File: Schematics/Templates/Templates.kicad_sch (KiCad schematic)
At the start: 2 parts, among them J1 Stack Male Edge Connector, U1 SAM-M8Q

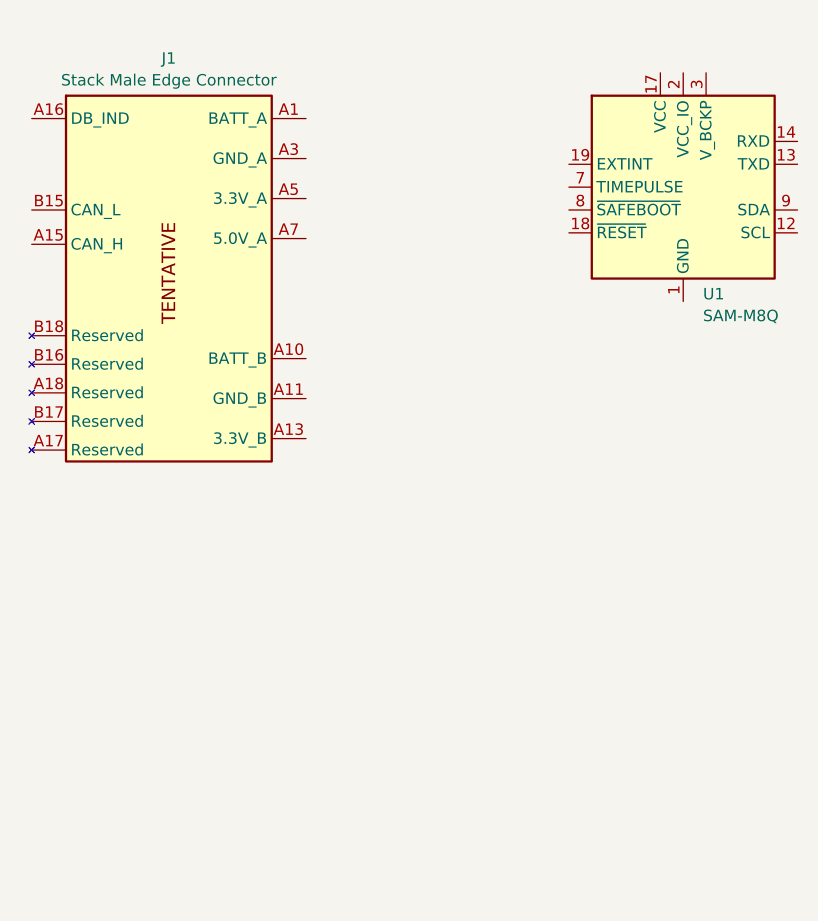
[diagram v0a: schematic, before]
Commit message: Added SWD programming header
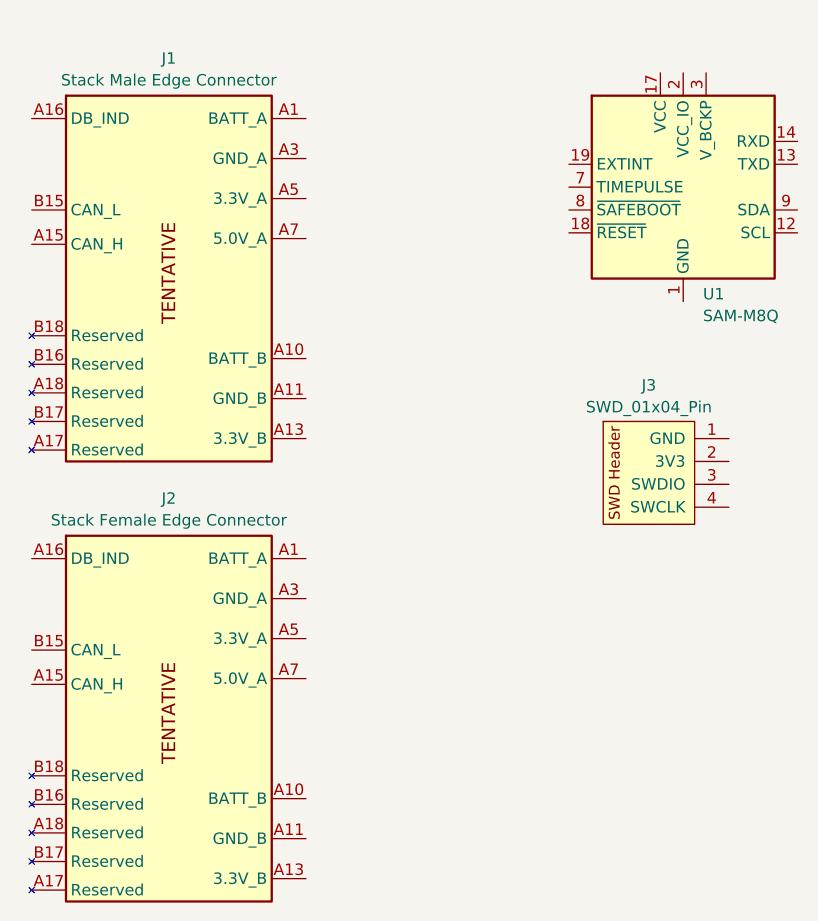
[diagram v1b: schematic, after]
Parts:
- added J2: Stack Female Edge Connector, footprints:CONN_10018784_AMP, symbol EdgeConnector:Stack Female Edge Connector
- added J3: SWD_01x04_Pin, SWD_Header:SWD_PinHeader_1x04_P2.54mm_Horizontal, symbol EdgeConnector:SWD_01x04_Pin
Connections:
- new net: J2.A1 (BATT_A), J2.A2 (BATT_A), J2.B1 (BATT_A), J2.B2 (BATT_A)
- new net: J2.A10 (BATT_B), J2.A9 (BATT_B), J2.B10 (BATT_B), J2.B9 (BATT_B)
- new net: J2.A11 (GND_B), J2.A12 (GND_B), J2.A14 (GND_B), J2.B11 (GND_B), J2.B12 (GND_B), J2.B14 (GND_B)
- new net: J2.A13 (3.3V_B), J2.B13 (3.3V_B)
- new net: J2.A3 (GND_A), J2.A4 (GND_A), J2.A6 (GND_A), J2.A8 (GND_A), J2.B3 (GND_A), J2.B4 (GND_A), J2.B6 (GND_A), J2.B8 (GND_A)
- new net: J2.A5 (3.3V_A), J2.B5 (3.3V_A)
- new net: J2.A7 (5.0V_A), J2.B7 (5.0V_A)
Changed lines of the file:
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@@
+    )
+  )
+  (symbol (lib_id "EdgeConnector:SWD_01x04_Pin") (at 107.95 67.31 0) (unit 1)
+    (in_bom yes) (on_board yes) (dnp no) (fields_autoplaced)
+    (property "Reference" "J3" (at 104.14 58.8477 0)
+      (effects (font (size 1.27 1.27)))
+    )
+    (property "Value" "SWD_01x04_Pin" (at 104.14 61.2719 0)
+      (effects (font (size 1.27 1.27)))
+    )
+    (property "Footprint" "SWD_Header:SWD_PinHeader_1x04_P2.54mm_Horizontal" (at 107.95 76.835 0)
+      (effects (font (size 1.27 1.27)) hide)
+    )
+    (property "Datasheet" "~" (at 99.06 75.565 0)
+      (effects (font (size 1.27 1.27)) hide)
+    )
+    (pin "1")
+    (pin "2")
+    (pin "3")
+    (pin "4")
+    (instances
+      (project "Templates"
+        (path "/89e89115-178c-4161-95c1-6f6deb6f4aa1"
+          (reference "J3") (unit 1)
+        )
+      )
     )
   )
@@
         )
       )
+    )
+  )
+  (symbol (lib_id "EdgeConnector:Stack Female Edge Connector") (at 50.8 97.155 0) (unit 1)
+    (in_bom yes) (on_board yes) (dnp no) (fields_autoplaced)
+    (property "Reference" "J2" (at 50.8 71.4207 0)
+      (effects (font (size 1.27 1.27)))
+    )
+    (property "Value" "Stack Female Edge Connector" (at 50.8 73.8449 0)
+      (effects (font (size 1.27 1.27)))
+    )
+    (property "Footprint" "footprints:CONN_10018784_AMP" (at 50.8 110.49 0)
+      (effects (font (size 1.27 1.27)) hide)
+    )
+    (property "Datasheet" "" (at 44.45 116.205 0)
+      (effects (font (size 1.27 1.27)) hide)
+    )
+    (pin "A1")
+    (pin "A10")
+    (pin "A11")
+    (pin "A12")
+    (pin "A13")
+    (pin "A14")
+    (pin "A15")
+    (pin "A16")
+    (pin "A17")
+    (pin "A18")
+    (pin "A2")
+    (pin "A3")
+    (pin "A4")
+    (pin "A5")
+    (pin "A6")
+    (pin "A7")
+    (pin "A8")
+    (pin "A9")
+    (pin "B1")
+    (pin "B10")
+    (pin "B11")
+    (pin "B12")
+    (pin "B13")
+    (pin "B14")
+    (pin "B15")
+    (pin "B16")
+    (pin "B17")
+    (pin "B18")
+    (pin "B2")
+    (pin "B3")
+    (pin "B4")
+    (pin "B5")
+    (pin "B6")
+    (pin "B7")
+    (pin "B8")
+    (pin "B9")
+    (instances
+      (project "Templates"
+        (path "/89e89115-178c-4161-95c1-6f6deb6f4aa1"
+          (reference "J2") (unit 1)
+        )
+      )

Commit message: Updated female edge connector footprint & model
Switched to the 10018784-10210TLF PCIe 1x female connector. Updated footprint appropriately, and added 3D model.
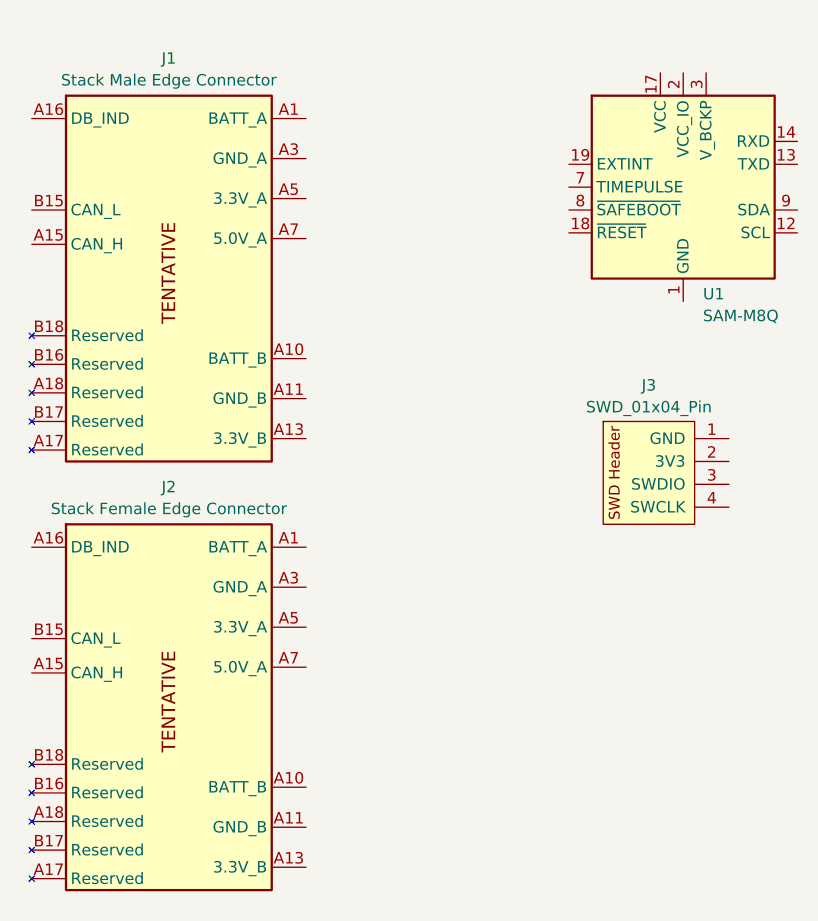
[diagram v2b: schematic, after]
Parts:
- J2: footprint footprints:CONN_10018784_AMP -> footprints:AMPHENOL_10018784-10210TLF
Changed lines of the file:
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@@
+    )
+  )
+  (symbol (lib_name "Stack Female Edge Connector_1") (lib_id "EdgeConnector:Stack Female Edge Connector") (at 50.8 95.885 0) (unit 1)
+    (in_bom yes) (on_board yes) (dnp no) (fields_autoplaced)
+    (property "Reference" "J2" (at 50.8 70.1507 0)
+      (effects (font (size 1.27 1.27)))
+    )
+    (property "Value" "Stack Female Edge Connector" (at 50.8 72.5749 0)
+      (effects (font (size 1.27 1.27)))
+    )
+    (property "Footprint" "footprints:AMPHENOL_10018784-10210TLF" (at 50.8 109.22 0)
+      (effects (font (size 1.27 1.27)) hide)
+    )
+    (property "Datasheet" "" (at 44.45 114.935 0)
+      (effects (font (size 1.27 1.27)) hide)
+    )
+    (pin "A1")
+    (pin "A10")
+    (pin "A11")
+    (pin "A12")
+    (pin "A13")
+    (pin "A14")
+    (pin "A15")
+    (pin "A16")
+    (pin "A17")
+    (pin "A18")
+    (pin "A2")
+    (pin "A3")
+    (pin "A4")
+    (pin "A5")
+    (pin "A6")
+    (pin "A7")
+    (pin "A8")
+    (pin "A9")
+    (pin "B1")
+    (pin "B10")
+    (pin "B11")
+    (pin "B12")
+    (pin "B13")
+    (pin "B14")
+    (pin "B15")
+    (pin "B16")
+    (pin "B17")
+    (pin "B18")
+    (pin "B2")
+    (pin "B3")
+    (pin "B4")
+    (pin "B5")
+    (pin "B6")
+    (pin "B7")
+    (pin "B8")
+    (pin "B9")
+    (instances
+      (project "Templates"
+        (path "/89e89115-178c-4161-95c1-6f6deb6f4aa1"
+          (reference "J2") (unit 1)
+        )
+      )
     )
   )
@@
         )
       )
-    )
-  )
-  (symbol (lib_id "EdgeConnector:Stack Female Edge Connector") (at 50.8 97.155 0) (unit 1)
-    (in_bom yes) (on_board yes) (dnp no) (fields_autoplaced)
-    (property "Reference" "J2" (at 50.8 71.4207 0)
-      (effects (font (size 1.27 1.27)))
-    )
-    (property "Value" "Stack Female Edge Connector" (at 50.8 73.8449 0)
-      (effects (font (size 1.27 1.27)))
-    )
-    (property "Footprint" "footprints:CONN_10018784_AMP" (at 50.8 110.49 0)
-      (effects (font (size 1.27 1.27)) hide)
-    )
-    (property "Datasheet" "" (at 44.45 116.205 0)
-      (effects (font (size 1.27 1.27)) hide)
-    )
-    (pin "A1")
-    (pin "A10")
-    (pin "A11")
-    (pin "A12")
-    (pin "A13")
-    (pin "A14")
-    (pin "A15")
-    (pin "A16")
-    (pin "A17")
-    (pin "A18")
-    (pin "A2")
-    (pin "A3")
-    (pin "A4")
-    (pin "A5")
-    (pin "A6")
-    (pin "A7")
-    (pin "A8")
-    (pin "A9")
-    (pin "B1")
-    (pin "B10")
-    (pin "B11")
-    (pin "B12")
-    (pin "B13")
-    (pin "B14")
-    (pin "B15")
-    (pin "B16")
-    (pin "B17")
-    (pin "B18")
-    (pin "B2")
-    (pin "B3")
-    (pin "B4")
-    (pin "B5")
-    (pin "B6")
-    (pin "B7")
-    (pin "B8")
-    (pin "B9")
-    (instances
-      (project "Templates"
-        (path "/89e89115-178c-4161-95c1-6f6deb6f4aa1"
-          (reference "J2") (unit 1)
-        )
-      )

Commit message: Removed keepout at front of PCB template
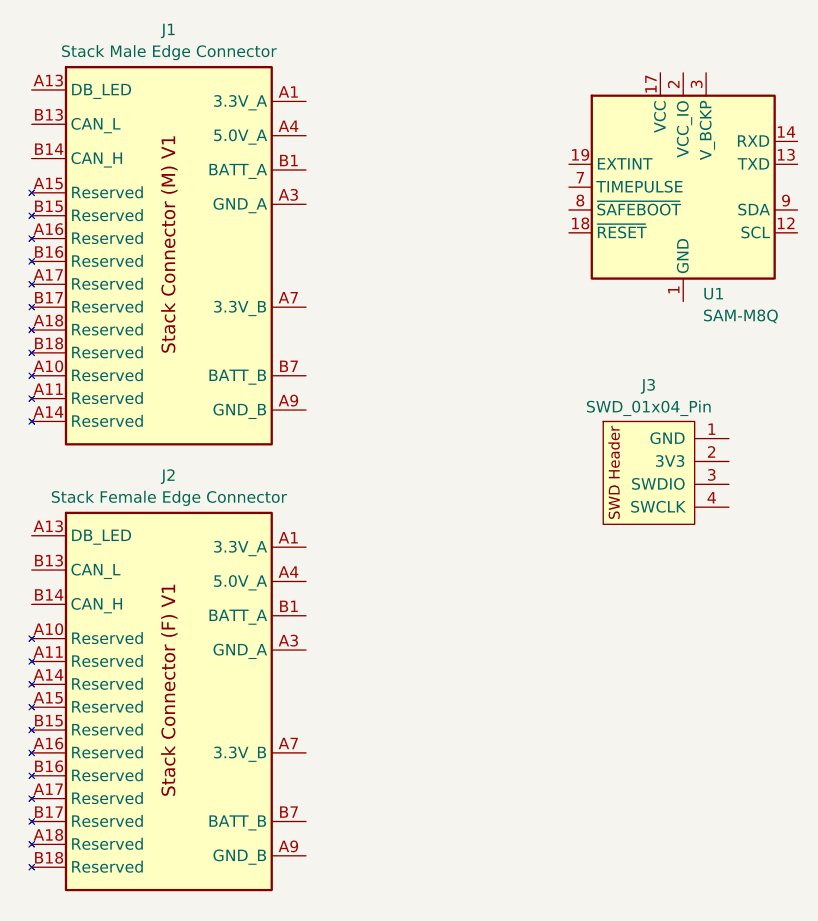
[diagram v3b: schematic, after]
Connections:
- net at J1.A1 (3.3V_A), J1.A2 (3.3V_A): no longer J1.B1 (BATT_A), J1.B2 (BATT_A)
- net at J1.A9 (GND_B), J1.B10 (GND_B): now also J1.A12 (GND_B), J1.B11 (GND_B), J1.B12 (GND_B); no longer J1.A10 (BATT_B), J1.B9 (BATT_B)
- net at J1.A13 (DB_LED): no longer J1.B13 (3.3V_B)
- net at J1.A3 (GND_A), J1.A6 (GND_A), J1.B4 (GND_A)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: now also J1.B5 (GND_A); no longer J1.A4 (GND_A), J1.A8 (GND_A), J1.B3 (GND_A), J1.B8 (GND_A)
- net 5.5V_A: now reaches J1.A5 (5.5V_A)
- net 5.5V_A: now also J1.A4 (5.0V_A), J2.A4 (5.0V_A), J2.A5 (5.5V_A); no longer J1.B5 (3.3V_A)
- net at J1.A7 (3.3V_B): now also J1.A8 (3.3V_B); no longer J1.B7 (5.0V_A)
- net at J2.A1 (3.3V_A), J2.A2 (3.3V_A): no longer J2.B1 (BATT_A), J2.B2 (BATT_A)
- net at J2.A9 (GND_B), J2.B10 (GND_B): now also J2.A12 (GND_B), J2.B11 (GND_B), J2.B12 (GND_B); no longer J2.A10 (BATT_B), J2.B9 (BATT_B)
- net at J2.A13 (DB_LED): no longer J2.B13 (3.3V_B)
- net at J2.A3 (GND_A), J2.A6 (GND_A), J2.B4 (GND_A)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: now also J2.B5 (GND_A); no longer J2.A4 (GND_A), J2.A8 (GND_A), J2.B3 (GND_A), J2.B8 (GND_A)
- net at J2.A7 (3.3V_B): now also J2.A8 (3.3V_B); no longer J2.B7 (5.0V_A)
- new net: J2.B1 (BATT_A), J2.B2 (BATT_A), J2.B3 (BATT_A)
- new net: J2.B7 (BATT_B), J2.B8 (BATT_B), J2.B9 (BATT_B)
- new net: J1.B1 (BATT_A), J1.B2 (BATT_A), J1.B3 (BATT_A)
- new net: J1.B7 (BATT_B), J1.B8 (BATT_B), J1.B9 (BATT_B)
- now unconnected: J1.A11 (GND_B), J1.A14 (GND_B), J1.B14 (GND_B), J2.A11 (GND_B), J2.A14 (GND_B), J2.B14 (GND_B)
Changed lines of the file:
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@@
 (kicad_sch (version 20230121) (generator eeschema)
   (paper "A4")
-  (symbol (lib_id "EdgeConnector:Stack Male Edge Connector") (at 50.8 48.26 0) (unit 1)
+  (symbol (lib_id "EdgeConnector:Stack Female Edge Connector") (at 50.8 94.615 0) (unit 1)
     (in_bom yes) (on_board yes) (dnp no) (fields_autoplaced)
-    (property "Reference" "J1" (at 50.8 22.5257 0)
+    (property "Reference" "J2" (at 50.8 68.8807 0)
       (effects (font (size 1.27 1.27)))
     )
-    (property "Value" "Stack Male Edge Connector" (at 50.8 24.9499 0)
+    (property "Value" "Stack Female Edge Connector" (at 50.8 71.3049 0)
       (effects (font (size 1.27 1.27)))
     )
-    (property "Footprint" "Connector_PCBEdge:BUS_PCIexpress_x1" (at 50.8 61.595 0)
+    (property "Footprint" "footprints:AMPHENOL_10018784-10210TLF" (at 50.8 117.475 0)
       (effects (font (size 1.27 1.27)) hide)
     )
-    (property "Datasheet" "" (at 44.45 67.31 0)
-      (effects (font (size 1.27 1.27)) hide)
-    )
-    (pin "A1")
-    (pin "A10")
-    (pin "A11")
-    (pin "A12")
-    (pin "A13")
-    (pin "A14")
-    (pin "A15")
-    (pin "A16")
-    (pin "A17")
-    (pin "A18")
-    (pin "A2")
-    (pin "A3")
-    (pin "A4")
-    (pin "A5")
-    (pin "A6")
-    (pin "A7")
-    (pin "A8")
-    (pin "A9")
-    (pin "B1")
-    (pin "B10")
-    (pin "B11")
-    (pin "B12")
-    (pin "B13")
-    (pin "B14")
-    (pin "B15")
-    (pin "B16")
-    (pin "B17")
-    (pin "B18")
-    (pin "B2")
-    (pin "B3")
-    (pin "B4")
-    (pin "B5")
-    (pin "B6")
-    (pin "B7")
-    (pin "B8")
-    (pin "B9")
-    (instances
-      (project "Templates"
-        (path "/89e89115-178c-4161-95c1-6f6deb6f4aa1"
-          (reference "J1") (unit 1)
-        )
-      )
-    )
-  )
-  (symbol (lib_name "Stack Female Edge Connector_1") (lib_id "EdgeConnector:Stack Female Edge Connector") (at 50.8 95.885 0) (unit 1)
-    (in_bom yes) (on_board yes) (dnp no) (fields_autoplaced)
-    (property "Reference" "J2" (at 50.8 70.1507 0)
-      (effects (font (size 1.27 1.27)))
-    )
-    (property "Value" "Stack Female Edge Connector" (at 50.8 72.5749 0)
-      (effects (font (size 1.27 1.27)))
-    )
-    (property "Footprint" "footprints:AMPHENOL_10018784-10210TLF" (at 50.8 109.22 0)
-      (effects (font (size 1.27 1.27)) hide)
-    )
-    (property "Datasheet" "" (at 44.45 114.935 0)
+    (property "Datasheet" "" (at 44.45 113.665 0)
       (effects (font (size 1.27 1.27)) hide)
     )
@@
         )
       )
+    )
+  )
+  (symbol (lib_name "Stack Male Edge Connector_1") (lib_id "EdgeConnector:Stack Male Edge Connector") (at 50.8 45.085 0) (unit 1)
+    (in_bom yes) (on_board yes) (dnp no) (fields_autoplaced)
+    (property "Reference" "J1" (at 50.8 19.3507 0)
+      (effects (font (size 1.27 1.27)))
+    )
+    (property "Value" "Stack Male Edge Connector" (at 50.8 21.7749 0)
+      (effects (font (size 1.27 1.27)))
+    )
+    (property "Footprint" "Connector_PCBEdge:BUS_PCIexpress_x1" (at 50.8 67.945 0)
+      (effects (font (size 1.27 1.27)) hide)
+    )
+    (property "Datasheet" "" (at 44.45 64.135 0)
+      (effects (font (size 1.27 1.27)) hide)
+    )
+    (pin "A1")
+    (pin "A10")
+    (pin "A11")
+    (pin "A12")
+    (pin "A13")
+    (pin "A14")
+    (pin "A15")
+    (pin "A16")
+    (pin "A17")
+    (pin "A18")
+    (pin "A2")
+    (pin "A3")
+    (pin "A4")
+    (pin "A5")
+    (pin "A6")
+    (pin "A7")
+    (pin "A8")
+    (pin "A9")
+    (pin "B1")
+    (pin "B10")
+    (pin "B11")
+    (pin "B12")
+    (pin "B13")
+    (pin "B14")
+    (pin "B15")
+    (pin "B16")
+    (pin "B17")
+    (pin "B18")
+    (pin "B2")
+    (pin "B3")
+    (pin "B4")
+    (pin "B5")
+    (pin "B6")
+    (pin "B7")
+    (pin "B8")
+    (pin "B9")
+    (instances
+      (project "Templates"
+        (path "/89e89115-178c-4161-95c1-6f6deb6f4aa1"
+          (reference "J1") (unit 1)
+        )
+      )
